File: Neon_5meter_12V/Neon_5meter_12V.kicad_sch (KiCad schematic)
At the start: 7 parts, among them U1 ESP32-WROOM-32, U2 XL1509-3.3

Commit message: updated schematic
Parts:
- added D11: LED_BGAR, LED_THT:LED_D5.0mm-4_RGB, symbol Device:LED_BGAR
- added D5: Blue LED, LED_SMD:LED_1206_3216Metric_Pad1.42x1.75mm_HandSolder, symbol Device:LED
- added D9: Red Power LED, LED_SMD:LED_1206_3216Metric_Pad1.42x1.75mm_HandSolder, symbol Device:LED
- added FID1, FID2: Fiducial, Fiducial:Fiducial_0.5mm_Mask1.5mm, symbol Mechanical:Fiducial
- added H1, H2: MountingHole_Pad, MountingHole:MountingHole_3.2mm_M3_Pad_Via, symbol Mechanical:MountingHole_Pad
- added J1, J3: Conn_01x16_Pin, Connector_PinHeader_2.54mm:PinHeader_1x16_P2.54mm_Vertical, symbol Connector:Conn_01x16_Pin
- added J2: +12V Jack, Connector_BarrelJack:BarrelJack_Horizontal, symbol Connector:Barrel_Jack_MountingPin
- added J4: Blue strip jack, Connector_BarrelJack:BarrelJack_Horizontal, symbol Connector:Barrel_Jack_MountingPin
- added J5: Pink strip Jack, Connector_BarrelJack:BarrelJack_Horizontal, symbol Connector:Barrel_Jack_MountingPin
- added J6: TSW-104-07-F-D, TSW-104-07-F-D:SAMTEC_TSW-104-07-F-D, symbol TSW-104-07-F-D:TSW-104-07-F-D
- added Q1, Q2: IRLML2502TRPBF, Package_TO_SOT_SMD:SOT-23, symbol Transistor_FET:BSS138
- added Q3, Q4, Q5: BSS138, Package_TO_SOT_SMD:SOT-23, symbol Transistor_FET:BSS138
- added R1: 2.2k Ohm, Resistor_SMD:R_1206_3216Metric_Pad1.30x1.75mm_HandSolder, symbol Device:R
- added R10, R13, R14, R15: 220 Ohm, Resistor_SMD:R_1206_3216Metric_Pad1.30x1.75mm_HandSolder, symbol Device:R
- added R11, R12: 130 Ohm, Resistor_SMD:R_1206_3216Metric_Pad1.30x1.75mm_HandSolder, symbol Device:R
- added R16, R17, R18, R3, R6: 10k Ohm, Resistor_SMD:R_1206_3216Metric_Pad1.30x1.75mm_HandSolder, symbol Device:R
- added R2, R5: 100 Ohm, Resistor_SMD:R_1206_3216Metric_Pad1.30x1.75mm_HandSolder, symbol Device:R
- added R4: 1k Ohm, Resistor_SMD:R_1206_3216Metric_Pad1.30x1.75mm_HandSolder, symbol Device:R
- C3: value 330uF 35V -> 330uF 50V
- D1: value D_Schottky -> 1N5822
- L1: value 47uH / 2A -> 47uH / 2A
- U1: link (none) -> https://uge-one.com/product/espressif-esp32-wroom-32-dual-c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
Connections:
- net +12V: now also D11.3 (A), J2.1, J4.1, J5.1
- net +3V3: now also U1.2 (VDD), J1.14 (Pin_14), J3.15 (Pin_15), J6.01, R1.2
- net GND: now also U1.1 (GND), U1.15 (GND), U1.38 (GND), U1.39 (GND), U2.4 (~{EN}), D5.1 (K), D9.1 (K), H1.1, H2.1, J1.15 (Pin_15), J2.2, J2.MP (MountPin), J3.16 (Pin_16), Q1.2 (S), Q2.2 (S), Q3.2 (S), Q4.2 (S), Q5.2 (S), R16.2, R17.2, R18.2, R3.2, R6.2
- net ESP_IO25: now reaches U1.10 (IO25)
- net ESP_IO25: now also J1.8 (Pin_8), R13.2
- net ESP_IO26: now reaches U1.11 (IO26)
- net ESP_IO26: now also J1.9 (Pin_9), R14.2
- net ESP_IO27: now reaches U1.12 (IO27)
- net ESP_IO27: now also J1.10 (Pin_10), R15.2
- net ESP_IO14: now reaches U1.13 (IO14)
- net ESP_IO14: now also J1.11 (Pin_11)
- net ESP_IO12: now reaches U1.14 (IO12)
- net ESP_IO12: now also J1.12 (Pin_12)
- net ESP_IO13: now reaches U1.16 (IO13)
- net ESP_IO13: now also J1.13 (Pin_13)
- net ESP_IO15: now reaches U1.23 (IO15)
- net ESP_IO15: now also J3.14 (Pin_14)
- net ESP_IO2: now reaches U1.24 (IO2)
- net ESP_IO2: now also J3.13 (Pin_13), R4.2
- net ESP_IO0: now reaches U1.25 (IO0)
- net ESP_IO0: now also J3.12 (Pin_12)
- net ESP_IO4: now reaches U1.26 (IO4)
- net ESP_IO4: now also J3.11 (Pin_11)
- net ESP_IO16: now reaches U1.27 (IO16)
- net ESP_IO16: now also J3.10 (Pin_10)
- net ESP_IO17: now reaches U1.28 (IO17)
- net ESP_IO17: now also J3.9 (Pin_9)
- net ESP_IO5: now reaches U1.29 (IO5)
- net ESP_IO5: now also J3.8 (Pin_8)
- net ESP_EN: now reaches U1.3 (EN)
- net ESP_EN: now also J1.1 (Pin_1)
- net ESP_IO18: now reaches U1.30 (IO18)
- net ESP_IO18: now also J3.7 (Pin_7), R2.2, R5.2
- net ESP_IO19: now reaches U1.31 (IO19)
- net ESP_IO19: now also J3.6 (Pin_6)
- net ESP_IO21: now reaches U1.33 (IO21)
- net ESP_IO21: now also J3.5 (Pin_5)
- net ESP_U0RX: now reaches U1.34 (RXD0/IO3)
- net ESP_U0RX: now also J3.4 (Pin_4), J6.02
- net ESP_U0TX: now reaches U1.35 (TXD0/IO1)
- net ESP_U0TX: now also J3.3 (Pin_3)
- net ESP_IO22: now reaches U1.36 (IO22)
- net ESP_IO22: now also J3.2 (Pin_2)
- net ESP_IO23: now reaches U1.37 (IO23)
- net ESP_IO23: now also J3.1 (Pin_1)
- net ESP_SVP: now reaches U1.4 (SENSOR_VP)
- net ESP_SVP: now also J1.2 (Pin_2)
- net ESP_SVN: now reaches U1.5 (SENSOR_VN)
- net ESP_SVN: now also J1.3 (Pin_3)
- net ESP_IO34: now reaches U1.6 (IO34)
- net ESP_IO34: now also J1.4 (Pin_4)
- net ESP_IO35: now reaches U1.7 (IO35)
- net ESP_IO35: now also J1.5 (Pin_5)
- net ESP_IO32: now reaches U1.8 (IO32)
- net ESP_IO32: now also J1.6 (Pin_6)
- net ESP_IO33: now reaches U1.9 (IO33)
- net ESP_IO33: now also J1.7 (Pin_7)
- new net: Q2.1 (G), R5.1, R6.1
- new net: Q3.1 (G), R13.1, R16.1
- new net: Q4.3 (D), R11.1
- new net: D11.2 (GK), R11.2
- new net: Q1.1 (G), R2.1, R3.1
- new net: Q5.3 (D), R12.1
- new net: D11.1 (BK), R12.2
- new net: Q5.1 (G), R15.1, R18.1
- new net: Q3.3 (D), R10.1
- new net: D11.4 (RK), R10.2
- new net: Q4.1 (G), R14.1, R17.1
- new net: D9.2 (A), R1.1
- new net: D5.2 (A), R4.1
- new net +5V: J1.16 (Pin_16)
- new net B_Jack: J4.2, J4.MP (MountPin), Q1.3 (D)
- new net P_Jack: J5.2, J5.MP (MountPin), Q2.3 (D)
- no-connect marks 0 -> 6
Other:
- note added: "12v RGB control using N channel Mosfet"
- note added: "BLUE LED, Vf=3V: V accross resistor = 3.3 - 3 = 0.3V I = V/R = 0.3/2200 = 0.59mAmp"
- note added: "DC-DC Buck Converter"
- note added: "ESP32-Wroom-32"
- note added: "Input 12v power jack Connector"
- note added: "LED Strip control using N channel Mosfet"
- note added: "LEDs"
- note added: "RED Power LED, Vf=2V: V accross resistor = 3.3 - 2 = 1.3V I = V/R = 1.3/1000 = 1.3mAmp"
- note added: "output Blue Color Jack"
- note added: "output Pink Color Jack"
- moved on the sheet: C1, C2, C3, D1, L1, U2

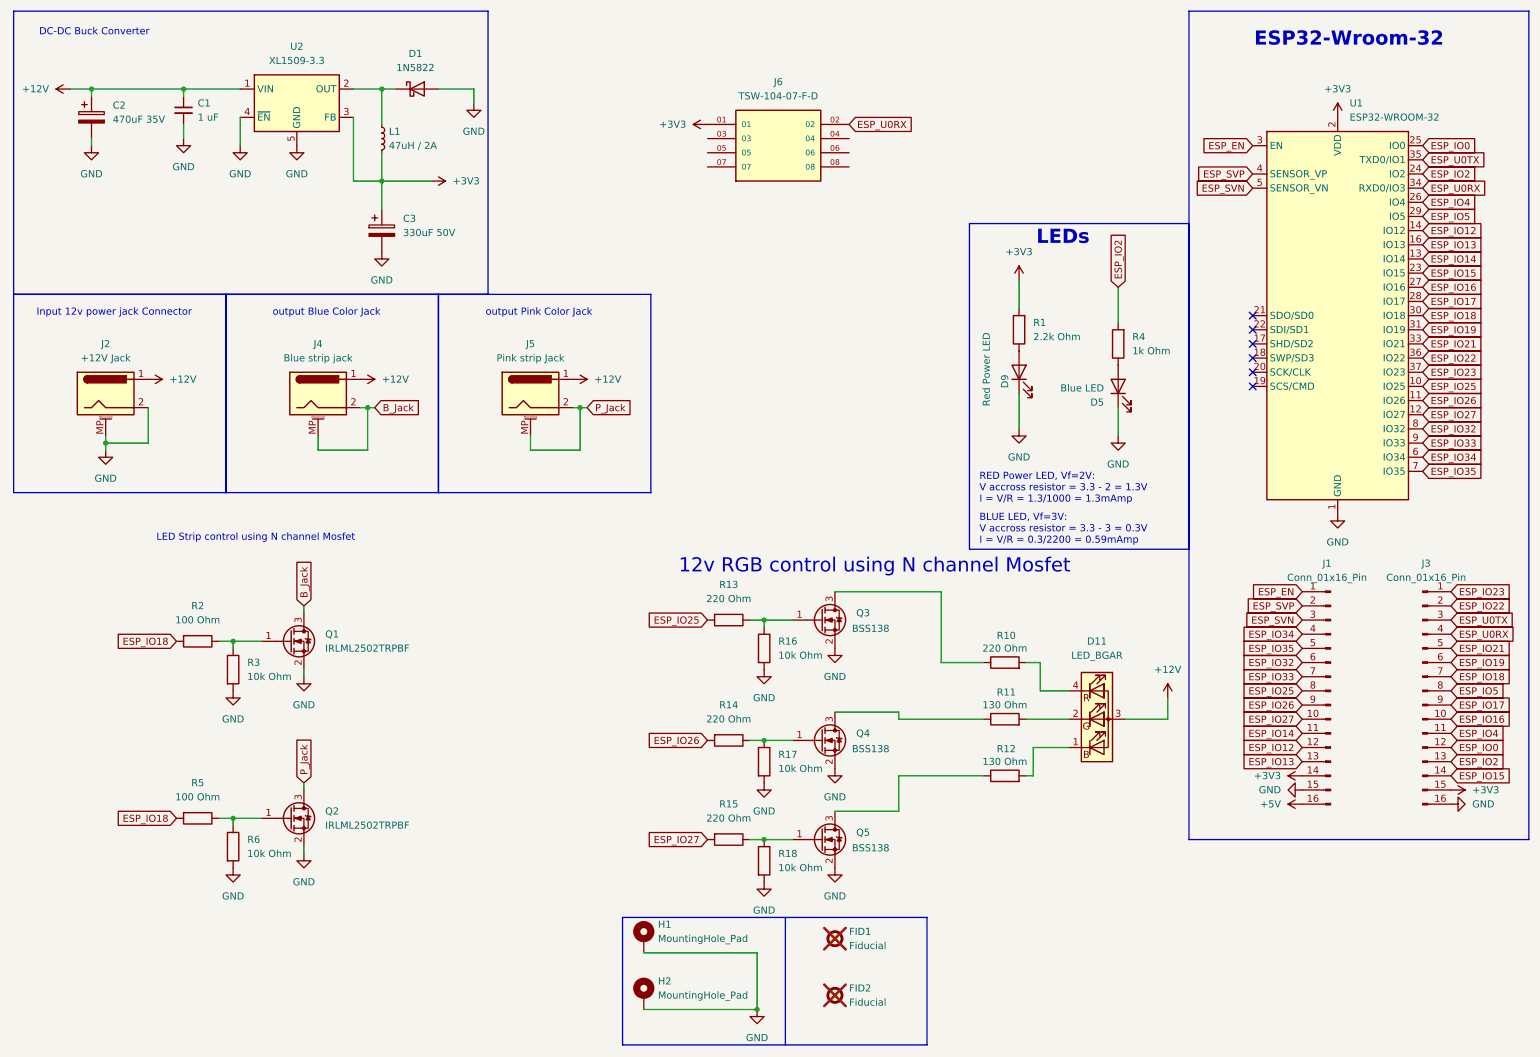
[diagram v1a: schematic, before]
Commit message: added external JST programmer connector
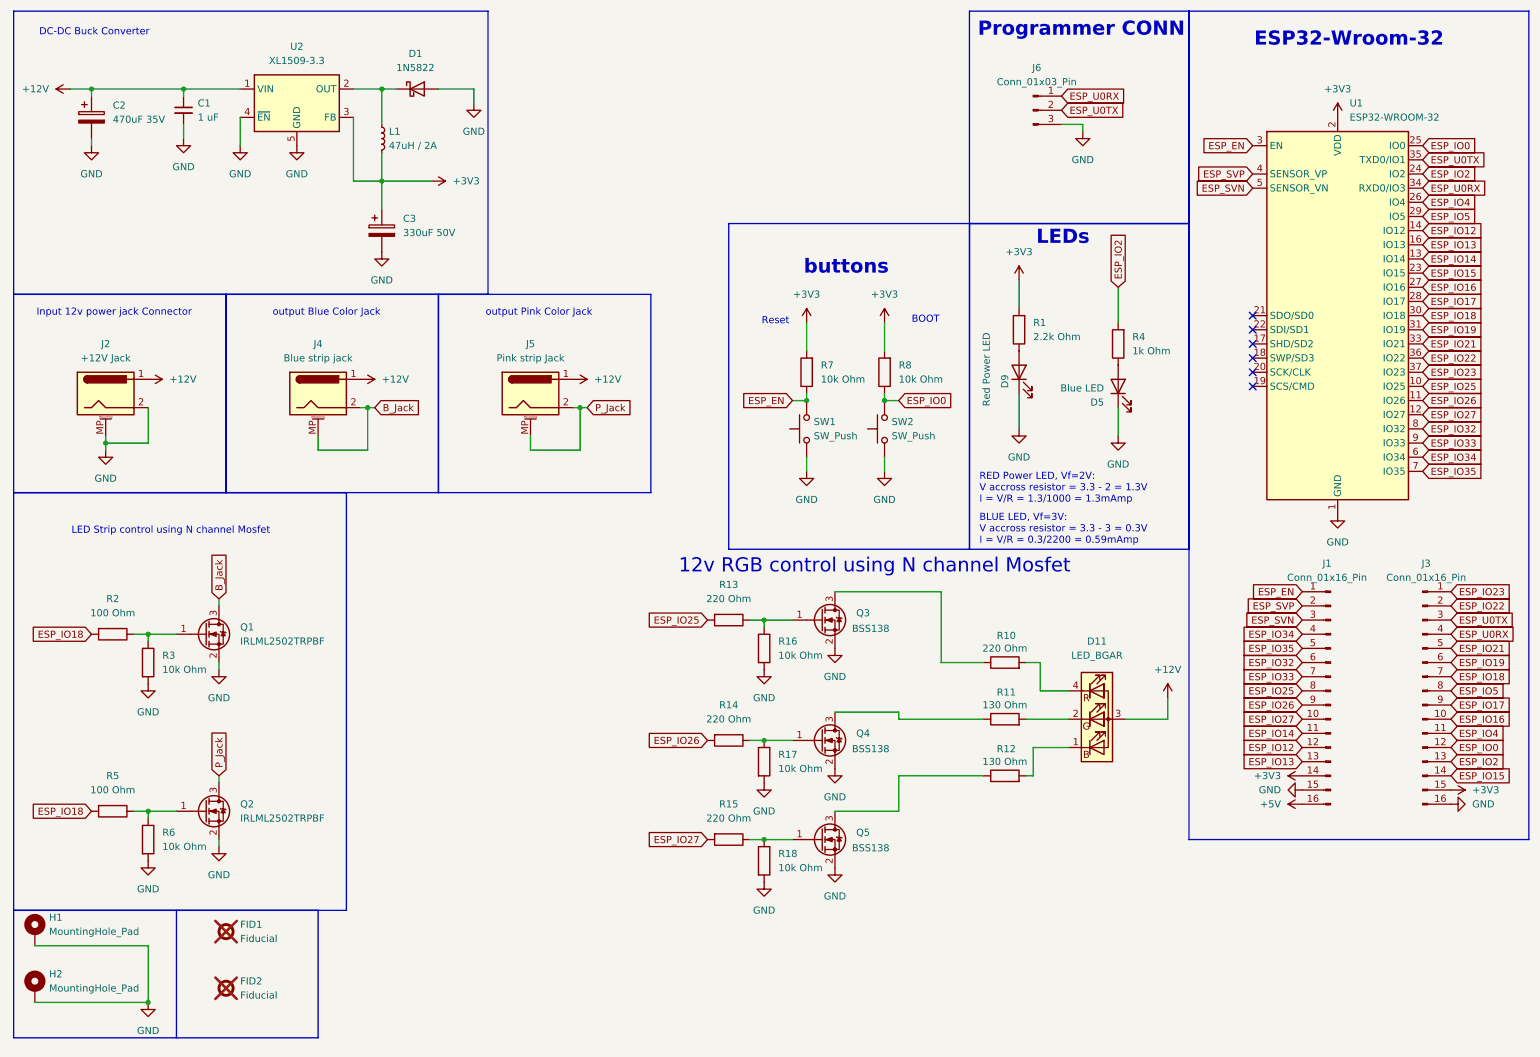
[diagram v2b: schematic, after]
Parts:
- removed J6: TSW-104-07-F-D, TSW-104-07-F-D:SAMTEC_TSW-104-07-F-D, symbol TSW-104-07-F-D:TSW-104-07-F-D
- added J6: Conn_01x03_Pin, Connector_PinHeader_2.54mm:PinHeader_1x03_P2.54mm_Horizontal, symbol Connector:Conn_01x03_Pin
- added R7, R8: 10k Ohm, Resistor_SMD:R_1206_3216Metric_Pad1.30x1.75mm_HandSolder, symbol Device:R
- added SW1, SW2: SW_Push, TS-1088-AR02016:SW_TS-1088-AR02016, symbol Switch:SW_Push
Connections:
- net +3V3: now also R7.2, R8.2
- net ESP_EN: now also R7.1, SW1.2
- net ESP_IO0: now also R8.1, SW2.2
- net ESP_U0RX: now also J6.1 (Pin_1)
- net ESP_U0TX: now also J6.2 (Pin_2)
- net GND: now also J6.3 (Pin_3), SW1.1, SW2.1
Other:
- note added: "BOOT"
- note added: "Programmer CONN"
- note added: "Reset"
- note added: "buttons"
- moved on the sheet: FID1, FID2, H1, H2, Q1, Q2, R2, R3, R5, R6
